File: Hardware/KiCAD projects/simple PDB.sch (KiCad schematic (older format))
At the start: 5 parts

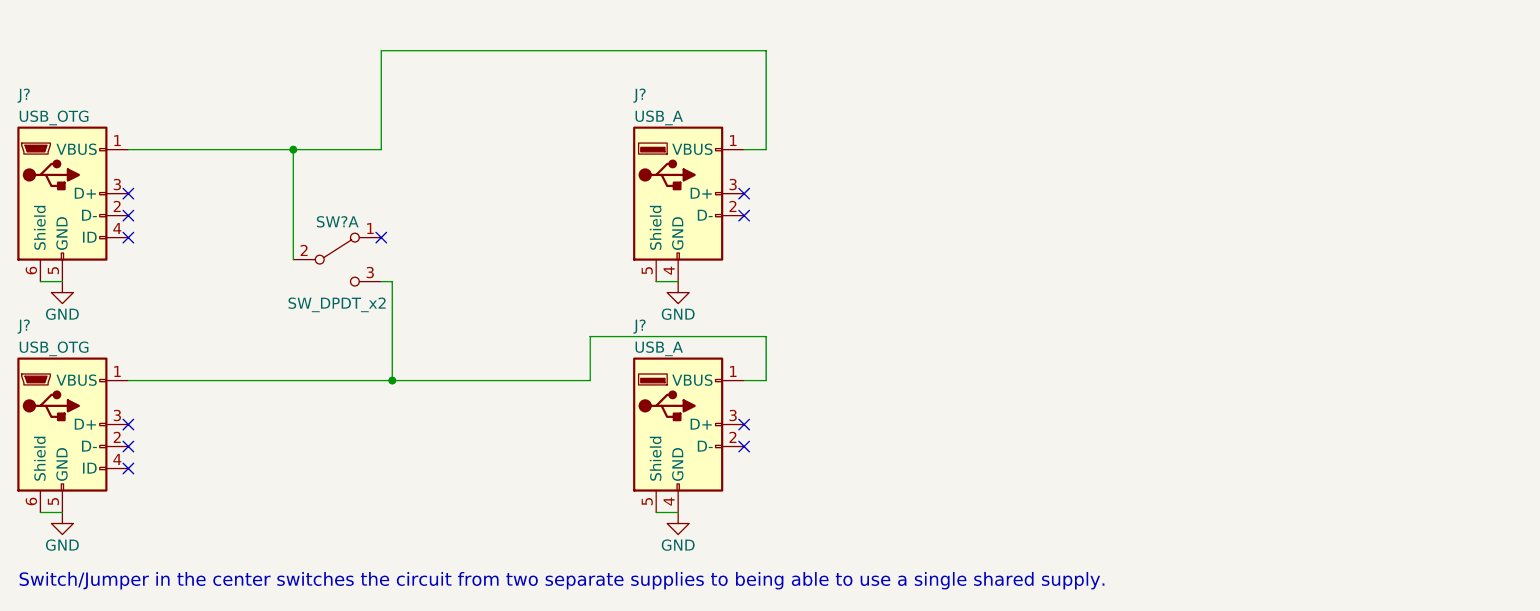
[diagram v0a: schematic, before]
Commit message: Added RPi setup instructions
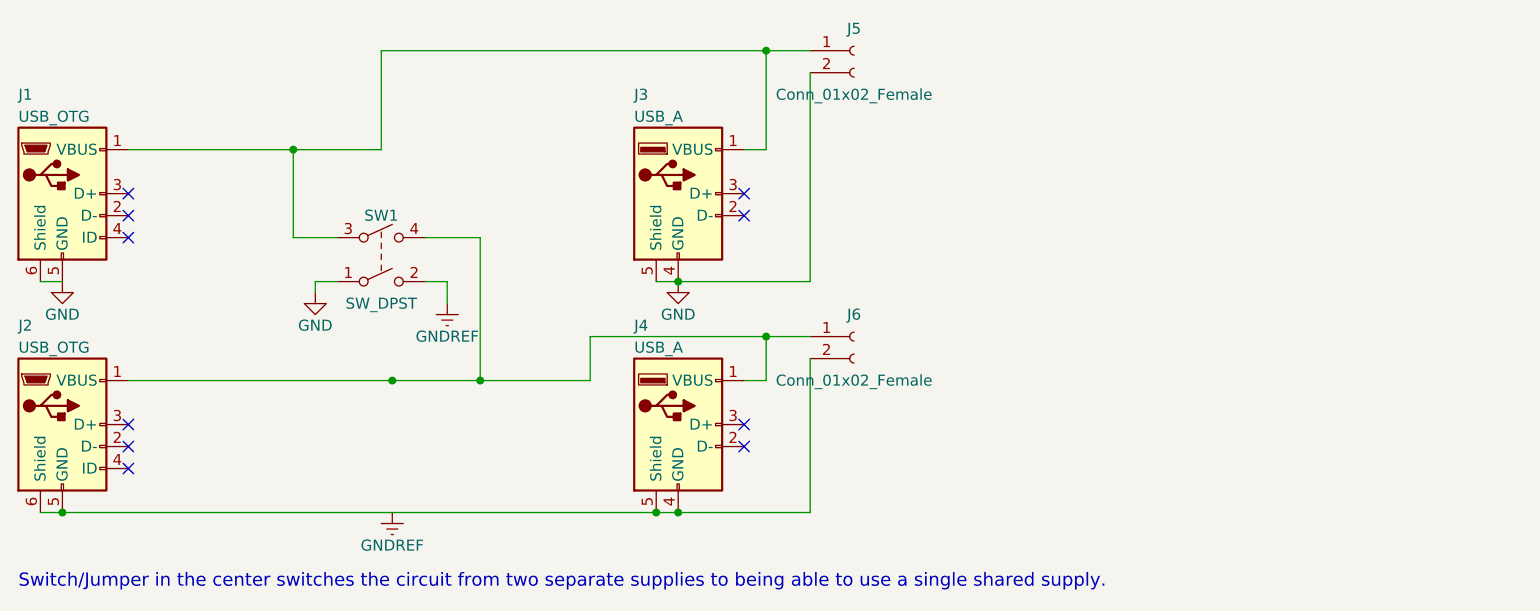
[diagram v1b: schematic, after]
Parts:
- removed SW?: SW_DPDT_x2, symbol SW_DPDT_x2
- added J5, J6: Conn_01x02_Female, symbol Conn_01x02_Female
- added SW1: SW_DPST, symbol SW_DPST
- gave numbers to parts that had none: 4
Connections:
- net GND: now also J5.2 (Pin_2), SW1.1; no longer J2.5 (GND), J2.6 (Shield), J4.4 (GND), J4.5 (Shield)
- net at J1.1 (VBUS), J3.1 (VBUS): now also J5.1 (Pin_1), SW1.3
- net at J2.1 (VBUS), J4.1 (VBUS): now also J6.1 (Pin_1), SW1.4
- new net: J2.5 (GND), J2.6 (Shield), J4.4 (GND), J4.5 (Shield), J6.2 (Pin_2)
- new net GNDREF: SW1.2
- no-connect marks 11 -> 10
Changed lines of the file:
@@
 LIBS:contrib
 LIBS:valves
+LIBS:simple PDB-cache
 EELAYER 25 0
 EELAYER END
@@
 $EndDescr
 $Comp
-L USB_OTG J?
+L USB_OTG J1
 U 1 1 5A3C0983
 P 3250 2050
-F 0 "J?" H 3050 2500 50  0000 L CNN
+F 0 "J1" H 3050 2500 50  0000 L CNN
 F 1 "USB_OTG" H 3050 2400 50  0000 L CNN
 F 2 "" H 3400 2000 50  0001 C CNN
@@
 $EndComp
 $Comp
-L USB_OTG J?
+L USB_OTG J2
 U 1 1 5A3C0AC4
 P 3250 3100
-F 0 "J?" H 3050 3550 50  0000 L CNN
+F 0 "J2" H 3050 3550 50  0000 L CNN
 F 1 "USB_OTG" H 3050 3450 50  0000 L CNN
 F 2 "" H 3400 3050 50  0001 C CNN
@@
 $EndComp
 $Comp
-L GND #PWR?
-U 1 1 5A3C0B41
-P 3250 3500
-F 0 "#PWR?" H 3250 3250 50  0001 C CNN
-F 1 "GND" H 3250 3350 50  0000 C CNN
-F 2 "" H 3250 3500 50  0001 C CNN
-F 3 "" H 3250 3500 50  0001 C CNN
-	1    3250 3500
-	1    0    0    -1
-$EndComp
-Wire Wire Line
-	3150 3500 3250 3500
-$Comp
-L GND #PWR?
-U 1 1 5A3C0B64
-P 3250 2450
-F 0 "#PWR?" H 3250 2200 50  0001 C CNN
-F 1 "GND" H 3250 2300 50  0000 C CNN
-F 2 "" H 3250 2450 50  0001 C CNN
-F 3 "" H 3250 2450 50  0001 C CNN
-	1    3250 2450
-	1    0    0    -1
-$EndComp
-Wire Wire Line
-	3150 2450 3250 2450
-$Comp
-L USB_A J?
+L USB_A J3
 U 1 1 5A3C0BC4
 P 6050 2050
-F 0 "J?" H 5850 2500 50  0000 L CNN
+F 0 "J3" H 5850 2500 50  0000 L CNN
 F 1 "USB_A" H 5850 2400 50  0000 L CNN
 F 2 "" H 6200 2000 50  0001 C CNN
@@
 $EndComp
 $Comp
-L USB_A J?
+L USB_A J4
 U 1 1 5A3C0C19
 P 6050 3100
-F 0 "J?" H 5850 3550 50  0000 L CNN
+F 0 "J4" H 5850 3550 50  0000 L CNN
 F 1 "USB_A" H 5850 3450 50  0000 L CNN
 F 2 "" H 6200 3050 50  0001 C CNN
@@
 	1    0    0    -1
 $EndComp
-$Comp
-L GND #PWR?
-U 1 1 5A3C0CE2
-P 6050 3500
-F 0 "#PWR?" H 6050 3250 50  0001 C CNN
-F 1 "GND" H 6050 3350 50  0000 C CNN
-F 2 "" H 6050 3500 50  0001 C CNN
-F 3 "" H 6050 3500 50  0001 C CNN
-	1    6050 3500
-	1    0    0    -1
-$EndComp
-Wire Wire Line
-	5950 3500 6050 3500
-$Comp
-L GND #PWR?
-U 1 1 5A3C0D0B
-P 6050 2450
-F 0 "#PWR?" H 6050 2200 50  0001 C CNN
-F 1 "GND" H 6050 2300 50  0000 C CNN
-F 2 "" H 6050 2450 50  0001 C CNN
-F 3 "" H 6050 2450 50  0001 C CNN
-	1    6050 2450
-	1    0    0    -1
-$EndComp
-Wire Wire Line
-	5950 2450 6050 2450
-Wire Wire Line
-	3550 1850 4700 1850
-Wire Wire Line
-	4700 1850 4700 1400
-Wire Wire Line
-	4700 1400 6450 1400
-Wire Wire Line
-	6450 1400 6450 1850
-Wire Wire Line
-	6450 1850 6350 1850
-Wire Wire Line
-	3550 2900 5650 2900
-Wire Wire Line
-	5650 2900 5650 2700
-Wire Wire Line
-	5650 2700 6450 2700
-Wire Wire Line
-	6450 2700 6450 2900
-Wire Wire Line
-	6450 2900 6350 2900
 NoConn ~ 3550 3100
 NoConn ~ 3550 3200
@@
 NoConn ~ 6350 3100
 NoConn ~ 6350 3200
-$Comp
-L SW_DPDT_x2 SW?
-U 1 1 5A3C0DA9
-P 4500 2350
-F 0 "SW?" H 4500 2520 50  0000 C CNN
-F 1 "SW_DPDT_x2" H 4500 2150 50  0000 C CNN
-F 2 "" H 4500 2350 50  0001 C CNN
-F 3 "" H 4500 2350 50  0001 C CNN
-	1    4500 2350
-	1    0    0    -1
-$EndComp
-Wire Wire Line
-	4300 2350 4300 1850
-Connection ~ 4300 1850
-Wire Wire Line
-	4700 2450 4750 2450
-Wire Wire Line
-	4750 2450 4750 2900
-Connection ~ 4750 2900
-NoConn ~ 4700 2250
 Text Notes 3050 3850 0    60   ~ 0
 Switch/Jumper in the center switches the circuit from two separate supplies to being able to use a single shared supply.\n
+$Comp
+L Conn_01x02_Female J5
+U 1 1 5A3C10C0
+P 6850 1400
+F 0 "J5" H 6850 1500 50  0000 C CNN
+F 1 "Conn_01x02_Female" H 6850 1200 50  0000 C CNN
+F 2 "" H 6850 1400 50  0001 C CNN
+F 3 "" H 6850 1400 50  0001 C CNN
+	1    6850 1400
+	1    0    0    -1
+$EndComp
+$Comp
+L Conn_01x02_Female J6
+U 1 1 5A3C1149
+P 6850 2700
+F 0 "J6" H 6850 2800 50  0000 C CNN
+F 1 "Conn_01x02_Female" H 6850 2500 50  0000 C CNN
+F 2 "" H 6850 2700 50  0001 C CNN
+F 3 "" H 6850 2700 50  0001 C CNN
+	1    6850 2700
+	1    0    0    -1
+$EndComp
+Wire Wire Line
+	3150 3500 6650 3500
+Wire Wire Line
+	3150 2450 3250 2450
+Wire Wire Line
+	5950 2450 6650 2450
+Wire Wire Line
+	3550 1850 4700 1850
+Wire Wire Line
+	4700 1850 4700 1400
+Wire Wire Line
+	4700 1400 6650 1400
+Wire Wire Line
+	6450 1400 6450 1850
+Wire Wire Line
+	6450 1850 6350 1850
+Wire Wire Line
+	3550 2900 5650 2900
+Wire Wire Line
+	5650 2900 5650 2700
+Wire Wire Line
+	5650 2700 6650 2700
+Wire Wire Line
+	6450 2700 6450 2900
+Wire Wire Line
+	6450 2900 6350 2900
+Connection ~ 4300 1850
+Connection ~ 4750 2900
+Connection ~ 6450 2700
+Wire Wire Line
+	6650 3500 6650 2800
+Connection ~ 6050 3500
+Connection ~ 6450 1400
+Wire Wire Line
+	6650 2450 6650 1500
+Connection ~ 6050 2450
+Connection ~ 5950 3500
+Connection ~ 3250 3500
+$Comp
+L GNDREF #PWR3
+U 1 1 5A3C15D3
+P 4750 3500
+F 0 "#PWR3" H 4750 3250 50  0001 C CNN
+F 1 "GNDREF" H 4750 3350 50  0000 C CNN
+F 2 "" H 4750 3500 50  0001 C CNN
+F 3 "" H 4750 3500 50  0001 C CNN
+	1    4750 3500
+	1    0    0    -1
+$EndComp
+$Comp
+L GND #PWR5
+U 1 1 5A3C15F5
+P 6050 2450
+F 0 "#PWR5" H 6050 2200 50  0001 C CNN
+F 1 "GND" H 6050 2300 50  0000 C CNN
+F 2 "" H 6050 2450 50  0001 C CNN
+F 3 "" H 6050 2450 50  0001 C CNN
+	1    6050 2450
+	1    0    0    -1
+$EndComp
+$Comp
+L GND #PWR1
+U 1 1 5A3C1617
+P 3250 2450
+F 0 "#PWR1" H 3250 2200 50  0001 C CNN
+F 1 "GND" H 3250 2300 50  0000 C CNN
+F 2 "" H 3250 2450 50  0001 C CNN
+F 3 "" H 3250 2450 50  0001 C CNN
+	1    3250 2450
+	1    0    0    -1
+$EndComp
+$Comp
+L SW_DPST SW1
+U 1 1 5A3C17A9
+P 4700 2350
+F 0 "SW1" H 4700 2550 50  0000 C CNN
+F 1 "SW_DPST" H 4700 2150 50  0000 C CNN
+F 2 "" H 4700 2350 50  0001 C CNN
+F 3 "" H 4700 2350 50  0001 C CNN
+	1    4700 2350
+	1    0    0    -1
+$EndComp
+Wire Wire Line
+	4300 1850 4300 2250
+Wire Wire Line
+	4300 2250 4500 2250
+Wire Wire Line
+	4900 2250 5150 2250
+Wire Wire Line
+	5150 2250 5150 2900
+Connection ~ 5150 2900
+$Comp
+L GND #PWR2
+U 1 1 5A3C18B6
+P 4400 2500
+F 0 "#PWR2" H 4400 2250 50  0001 C CNN
+F 1 "GND" H 4400 2350 50  0000 C CNN
+F 2 "" H 4400 2500 50  0001 C CNN
+F 3 "" H 4400 2500 50  0001 C CNN
+	1    4400 2500
+	1    0    0    -1
+$EndComp
+Wire Wire Line
+	4400 2500 4400 2450
+Wire Wire Line
+	4400 2450 4500 2450
+$Comp
+L GNDREF #PWR4
+U 1 1 5A3C1908
+P 5000 2550
+F 0 "#PWR4" H 5000 2300 50  0001 C CNN
+F 1 "GNDREF" H 5000 2400 50  0000 C CNN
+F 2 "" H 5000 2550 50  0001 C CNN
+F 3 "" H 5000 2550 50  0001 C CNN
+	1    5000 2550
+	1    0    0    -1
+$EndComp
+Wire Wire Line
+	4900 2450 5000 2450
+Wire Wire Line
+	5000 2450 5000 2550
 $EndSCHEMATC
